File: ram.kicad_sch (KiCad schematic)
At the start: 8 parts, among them J1 ramslot1, J2 ramslot2, J3 ramslot3, J4 ramslot4, U24 74HC08, U29 74HC32, U30 74HC139

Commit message: done the pcb layout + added the 1M ram bank project
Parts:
- U24, U29: footprint Package_DIP:DIP-14_W7.62mm_Socket -> Package_DIP:DIP-14_W7.62mm
- U30: footprint (none) -> Package_DIP:DIP-16_W7.62mm
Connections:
- net BKE_{1} is gone; now on net ~{DRD}: J2.43 (Pin_43), U30.5 (O1)
- net A_{10}: now also J1.11 (Pin_11), J2.11 (Pin_11), J3.11 (Pin_11), J4.11 (Pin_11); no longer J1.12 (Pin_12), J2.12 (Pin_12), J3.12 (Pin_12), J4.12 (Pin_12)
- net A_{11}: now also J1.14 (Pin_14), J2.14 (Pin_14), J3.14 (Pin_14), J4.14 (Pin_14); no longer J1.13 (Pin_13), J2.13 (Pin_13), J3.13 (Pin_13), J4.13 (Pin_13)
- net A_{1}: now also J1.4 (Pin_4), J2.4 (Pin_4), J3.4 (Pin_4), J4.4 (Pin_4); no longer J1.3 (Pin_3), J2.3 (Pin_3), J3.3 (Pin_3), J4.3 (Pin_3)
- net A_{2}: now also J1.3 (Pin_3), J2.3 (Pin_3), J3.3 (Pin_3), J4.3 (Pin_3); no longer J1.4 (Pin_4), J2.4 (Pin_4), J3.4 (Pin_4), J4.4 (Pin_4)
- net A_{3}: now also J1.6 (Pin_6), J2.6 (Pin_6), J3.6 (Pin_6), J4.6 (Pin_6); no longer J1.5 (Pin_5), J2.5 (Pin_5), J3.5 (Pin_5), J4.5 (Pin_5)
- net A_{4}: now also J1.5 (Pin_5), J2.5 (Pin_5), J3.5 (Pin_5), J4.5 (Pin_5); no longer J1.6 (Pin_6), J2.6 (Pin_6), J3.6 (Pin_6), J4.6 (Pin_6)
- net A_{5}: now also J1.8 (Pin_8), J2.8 (Pin_8), J3.8 (Pin_8), J4.8 (Pin_8); no longer J1.7 (Pin_7), J2.7 (Pin_7), J3.7 (Pin_7), J4.7 (Pin_7)
- net A_{6}: now also J1.7 (Pin_7), J2.7 (Pin_7), J3.7 (Pin_7), J4.7 (Pin_7); no longer J1.8 (Pin_8), J2.8 (Pin_8), J3.8 (Pin_8), J4.8 (Pin_8)
- net A_{7}: now also J1.10 (Pin_10), J2.10 (Pin_10), J3.10 (Pin_10), J4.10 (Pin_10); no longer J1.9 (Pin_9), J2.9 (Pin_9), J3.9 (Pin_9), J4.9 (Pin_9)
- net A_{8}: now also J1.9 (Pin_9), J2.9 (Pin_9), J3.9 (Pin_9), J4.9 (Pin_9); no longer J1.10 (Pin_10), J2.10 (Pin_10), J3.10 (Pin_10), J4.10 (Pin_10)
- net A_{9}: now also J1.12 (Pin_12), J2.12 (Pin_12), J3.12 (Pin_12), J4.12 (Pin_12); no longer J1.11 (Pin_11), J2.11 (Pin_11), J3.11 (Pin_11), J4.11 (Pin_11)
- net DS.~{L}: now also J1.47 (Pin_47), J2.47 (Pin_47), J3.47 (Pin_47), J4.47 (Pin_47); no longer J1.48 (Pin_48), J2.48 (Pin_48), J3.48 (Pin_48), J4.48 (Pin_48)
- net DS.~{U}: now also J1.48 (Pin_48), J2.48 (Pin_48), J3.48 (Pin_48), J4.48 (Pin_48); no longer J1.47 (Pin_47), J2.47 (Pin_47), J3.47 (Pin_47), J4.47 (Pin_47)
- net D_{0}: now also J1.26 (Pin_26), J2.26 (Pin_26), J3.26 (Pin_26), J4.26 (Pin_26); no longer J1.25 (Pin_25), J2.25 (Pin_25), J3.25 (Pin_25), J4.25 (Pin_25)
- net D_{10}: now also J1.36 (Pin_36), J2.36 (Pin_36), J3.36 (Pin_36), J4.36 (Pin_36); no longer J1.35 (Pin_35), J2.35 (Pin_35), J3.35 (Pin_35), J4.35 (Pin_35)
- net D_{11}: now also J1.35 (Pin_35), J2.35 (Pin_35), J3.35 (Pin_35), J4.35 (Pin_35); no longer J1.36 (Pin_36), J2.36 (Pin_36), J3.36 (Pin_36), J4.36 (Pin_36)
- net D_{12}: now also J1.38 (Pin_38), J2.38 (Pin_38), J3.38 (Pin_38), J4.38 (Pin_38); no longer J1.37 (Pin_37), J2.37 (Pin_37), J3.37 (Pin_37), J4.37 (Pin_37)
- net D_{13}: now also J1.37 (Pin_37), J2.37 (Pin_37), J3.37 (Pin_37), J4.37 (Pin_37); no longer J1.38 (Pin_38), J2.38 (Pin_38), J3.38 (Pin_38), J4.38 (Pin_38)
- net D_{14}: now also J1.40 (Pin_40), J2.40 (Pin_40), J3.40 (Pin_40), J4.40 (Pin_40); no longer J1.39 (Pin_39), J2.39 (Pin_39), J3.39 (Pin_39), J4.39 (Pin_39)
- net D_{15}: now also J1.39 (Pin_39), J2.39 (Pin_39), J3.39 (Pin_39), J4.39 (Pin_39); no longer J1.40 (Pin_40), J2.40 (Pin_40), J3.40 (Pin_40), J4.40 (Pin_40)
- net D_{1}: now also J1.25 (Pin_25), J2.25 (Pin_25), J3.25 (Pin_25), J4.25 (Pin_25); no longer J1.26 (Pin_26), J2.26 (Pin_26), J3.26 (Pin_26), J4.26 (Pin_26)
- net D_{2}: now also J1.28 (Pin_28), J2.28 (Pin_28), J3.28 (Pin_28), J4.28 (Pin_28); no longer J1.27 (Pin_27), J2.27 (Pin_27), J3.27 (Pin_27), J4.27 (Pin_27)
- net D_{3}: now also J1.27 (Pin_27), J2.27 (Pin_27), J3.27 (Pin_27), J4.27 (Pin_27); no longer J1.28 (Pin_28), J2.28 (Pin_28), J3.28 (Pin_28), J4.28 (Pin_28)
- net D_{4}: now also J1.30 (Pin_30), J2.30 (Pin_30), J3.30 (Pin_30), J4.30 (Pin_30); no longer J1.29 (Pin_29), J2.29 (Pin_29), J3.29 (Pin_29), J4.29 (Pin_29)
- net D_{5}: now also J1.29 (Pin_29), J2.29 (Pin_29), J3.29 (Pin_29), J4.29 (Pin_29); no longer J1.30 (Pin_30), J2.30 (Pin_30), J3.30 (Pin_30), J4.30 (Pin_30)
- net D_{6}: now also J1.32 (Pin_32), J2.32 (Pin_32), J3.32 (Pin_32), J4.32 (Pin_32); no longer J1.31 (Pin_31), J2.31 (Pin_31), J3.31 (Pin_31), J4.31 (Pin_31)
- net D_{7}: now also J1.31 (Pin_31), J2.31 (Pin_31), J3.31 (Pin_31), J4.31 (Pin_31); no longer J1.32 (Pin_32), J2.32 (Pin_32), J3.32 (Pin_32), J4.32 (Pin_32)
- net D_{8}: now also J1.34 (Pin_34), J2.34 (Pin_34), J3.34 (Pin_34), J4.34 (Pin_34); no longer J1.33 (Pin_33), J2.33 (Pin_33), J3.33 (Pin_33), J4.33 (Pin_33)
- net D_{9}: now also J1.33 (Pin_33), J2.33 (Pin_33), J3.33 (Pin_33), J4.33 (Pin_33); no longer J1.34 (Pin_34), J2.34 (Pin_34), J3.34 (Pin_34), J4.34 (Pin_34)
- net E_{0}: now also J1.21 (Pin_21), J2.21 (Pin_21), J3.21 (Pin_21), J4.21 (Pin_21); no longer J1.22 (Pin_22), J2.22 (Pin_22), J3.22 (Pin_22), J4.22 (Pin_22)
- net E_{10}: now also J1.15 (Pin_15), J2.15 (Pin_15), J3.15 (Pin_15), J4.15 (Pin_15); no longer J1.16 (Pin_16), J2.16 (Pin_16), J3.16 (Pin_16), J4.16 (Pin_16)
- net E_{11}: now also J1.18 (Pin_18), J2.18 (Pin_18), J3.18 (Pin_18), J4.18 (Pin_18); no longer J1.17 (Pin_17), J2.17 (Pin_17), J3.17 (Pin_17), J4.17 (Pin_17)
- net E_{12}: now also J1.17 (Pin_17), J2.17 (Pin_17), J3.17 (Pin_17), J4.17 (Pin_17); no longer J1.18 (Pin_18), J2.18 (Pin_18), J3.18 (Pin_18), J4.18 (Pin_18)
- net E_{13}: now also J1.20 (Pin_20), J2.20 (Pin_20), J3.20 (Pin_20), J4.20 (Pin_20); no longer J1.19 (Pin_19), J2.19 (Pin_19), J3.19 (Pin_19), J4.19 (Pin_19)
- net E_{14}: now also J1.19 (Pin_19), J2.19 (Pin_19), J3.19 (Pin_19), J4.19 (Pin_19); no longer J1.20 (Pin_20), J2.20 (Pin_20), J3.20 (Pin_20), J4.20 (Pin_20)
- net E_{15}: now also J1.22 (Pin_22), J2.22 (Pin_22), J3.22 (Pin_22), J4.22 (Pin_22); no longer J1.21 (Pin_21), J2.21 (Pin_21), J3.21 (Pin_21), J4.21 (Pin_21)
- net E_{1}: now also J1.24 (Pin_24), J2.24 (Pin_24), J3.24 (Pin_24), J4.24 (Pin_24); no longer J1.23 (Pin_23), J2.23 (Pin_23), J3.23 (Pin_23), J4.23 (Pin_23)
- net E_{8}: now also J1.13 (Pin_13), J2.13 (Pin_13), J3.13 (Pin_13), J4.13 (Pin_13); no longer J1.14 (Pin_14), J2.14 (Pin_14), J3.14 (Pin_14), J4.14 (Pin_14)
- net E_{9}: now also J1.16 (Pin_16), J2.16 (Pin_16), J3.16 (Pin_16), J4.16 (Pin_16); no longer J1.15 (Pin_15), J2.15 (Pin_15), J3.15 (Pin_15), J4.15 (Pin_15)
- net GND: now also J1.23 (Pin_23), J2.23 (Pin_23), J3.23 (Pin_23), J4.23 (Pin_23); no longer J1.24 (Pin_24), J2.24 (Pin_24), J3.24 (Pin_24), J4.24 (Pin_24)
- net PDIR.~{R}: now also J1.45 (Pin_45), J2.45 (Pin_45), J3.45 (Pin_45), J4.45 (Pin_45); no longer J1.46 (Pin_46), J2.46 (Pin_46), J3.46 (Pin_46), J4.46 (Pin_46)
- net PDIR.~{W}: now also J1.46 (Pin_46), J2.46 (Pin_46), J3.46 (Pin_46), J4.46 (Pin_46); no longer J1.45 (Pin_45), J2.45 (Pin_45), J3.45 (Pin_45), J4.45 (Pin_45)
- net ~{DRD}: now also J1.43 (Pin_43), J3.43 (Pin_43), J4.43 (Pin_43); no longer J1.44 (Pin_44), J3.44 (Pin_44), J4.44 (Pin_44)
- net BKE_{0} renamed ~{BKE_{0}}
- net ~{BKE_{0}}: now also J1.44 (Pin_44); no longer J1.43 (Pin_43)
- net BKE_{2} renamed ~{BKE_{2}}
- net ~{BKE_{2}}: now also J3.44 (Pin_44); no longer J3.43 (Pin_43)
- net BKE_{3} renamed ~{BKE_{3}}
- net ~{BKE_{3}}: now also J4.44 (Pin_44); no longer J4.43 (Pin_43)

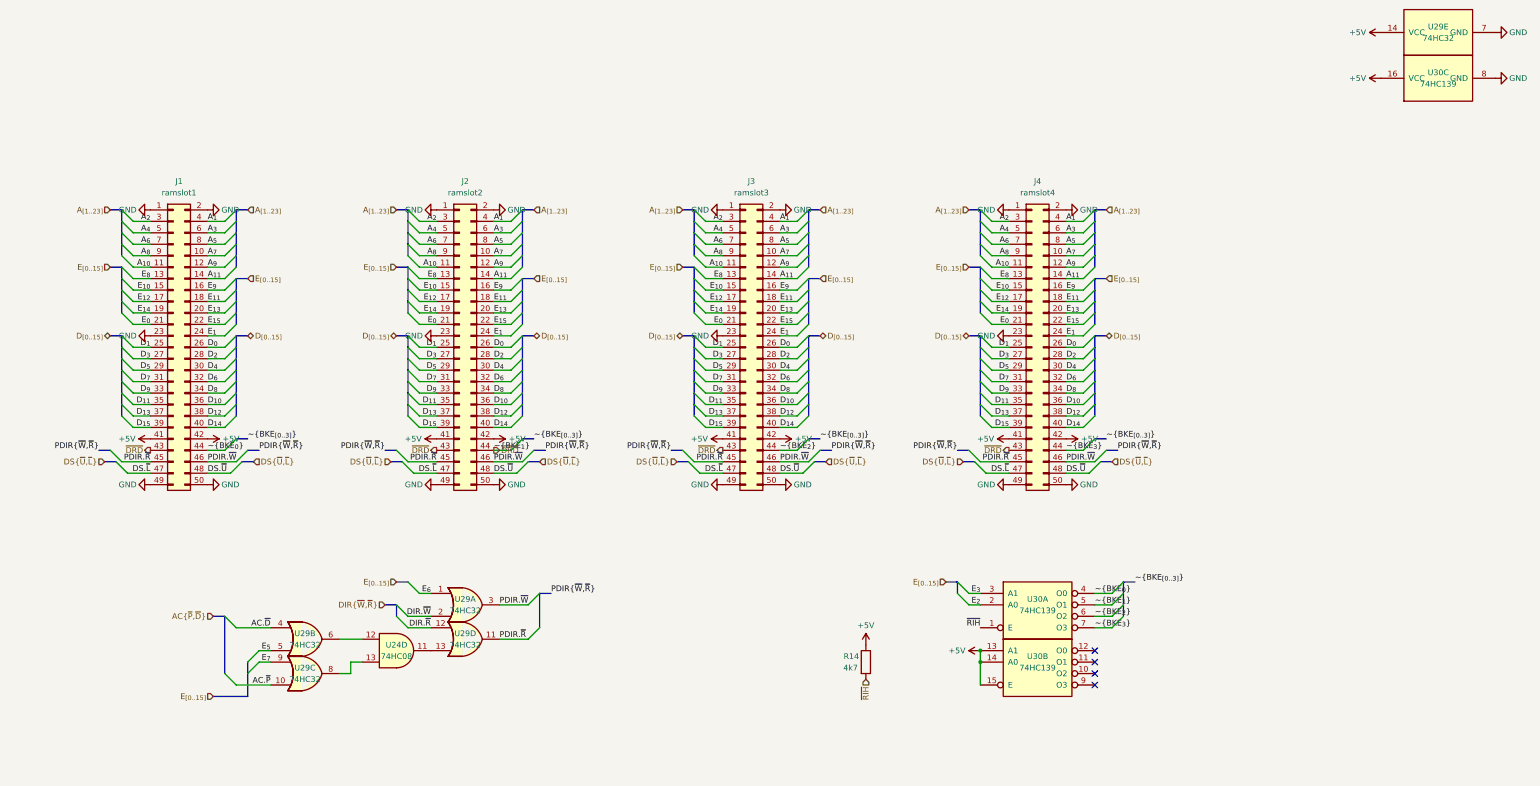
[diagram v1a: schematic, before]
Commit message: updated scheme: 	- fixed E to P & PRT mapping 	- swapped root's 04 couple with the 14's of pidreg & statusreg
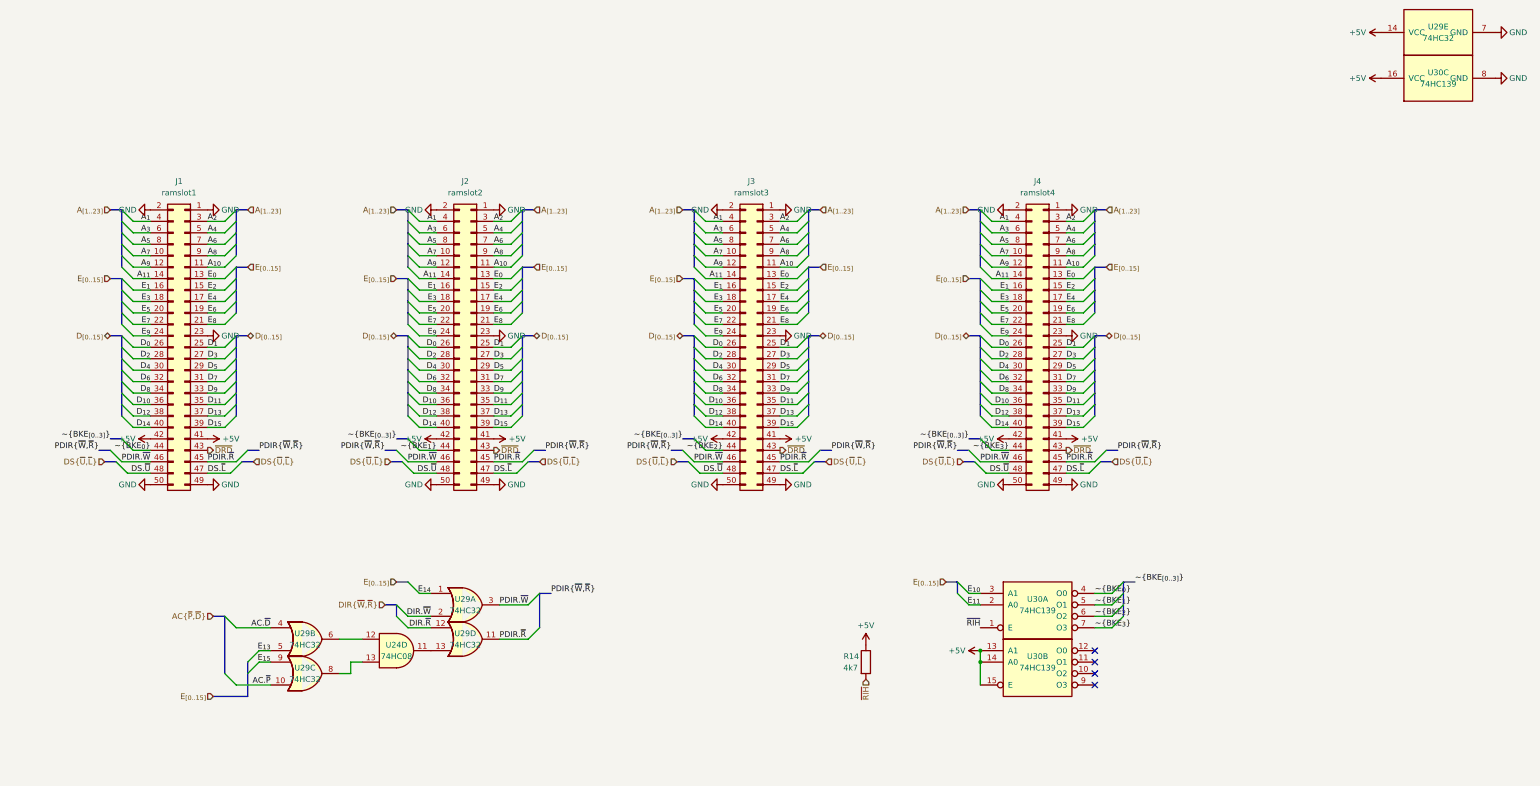
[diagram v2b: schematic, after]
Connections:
- net E_{0}: now also J1.13 (Pin_13), J2.13 (Pin_13), J3.13 (Pin_13), J4.13 (Pin_13); no longer J1.21 (Pin_21), J2.21 (Pin_21), J3.21 (Pin_21), J4.21 (Pin_21)
- net E_{10}: now also U30.3 (A1); no longer J1.15 (Pin_15), J2.15 (Pin_15), J3.15 (Pin_15), J4.15 (Pin_15)
- net E_{11}: now also U30.2 (A0); no longer J1.18 (Pin_18), J2.18 (Pin_18), J3.18 (Pin_18), J4.18 (Pin_18)
- net E_{13}: now also U29.5; no longer J1.20 (Pin_20), J2.20 (Pin_20), J3.20 (Pin_20), J4.20 (Pin_20)
- net E_{14}: now also U29.1; no longer J1.19 (Pin_19), J2.19 (Pin_19), J3.19 (Pin_19), J4.19 (Pin_19)
- net E_{15}: now also U29.9; no longer J1.22 (Pin_22), J2.22 (Pin_22), J3.22 (Pin_22), J4.22 (Pin_22)
- net E_{1}: now also J1.16 (Pin_16), J2.16 (Pin_16), J3.16 (Pin_16), J4.16 (Pin_16); no longer J1.24 (Pin_24), J2.24 (Pin_24), J3.24 (Pin_24), J4.24 (Pin_24)
- net E_{2}: now also J1.15 (Pin_15), J2.15 (Pin_15), J3.15 (Pin_15), J4.15 (Pin_15); no longer U30.2 (A0)
- net E_{3}: now also J1.18 (Pin_18), J2.18 (Pin_18), J3.18 (Pin_18), J4.18 (Pin_18); no longer U30.3 (A1)
- net E_{5}: now also J1.20 (Pin_20), J2.20 (Pin_20), J3.20 (Pin_20), J4.20 (Pin_20); no longer U29.5
- net E_{6}: now also J1.19 (Pin_19), J2.19 (Pin_19), J3.19 (Pin_19), J4.19 (Pin_19); no longer U29.1
- net E_{7}: now also J1.22 (Pin_22), J2.22 (Pin_22), J3.22 (Pin_22), J4.22 (Pin_22); no longer U29.9
- net E_{8}: now also J1.21 (Pin_21), J2.21 (Pin_21), J3.21 (Pin_21), J4.21 (Pin_21); no longer J1.13 (Pin_13), J2.13 (Pin_13), J3.13 (Pin_13), J4.13 (Pin_13)
- net E_{9}: now also J1.24 (Pin_24), J2.24 (Pin_24), J3.24 (Pin_24), J4.24 (Pin_24); no longer J1.16 (Pin_16), J2.16 (Pin_16), J3.16 (Pin_16), J4.16 (Pin_16)
- net ~{DRD}: no longer J2.44 (Pin_44), U30.5 (O1)
- net E_{12} renamed E_{4}
- new net ~{BKE_{1}}: J2.44 (Pin_44), U30.5 (O1)

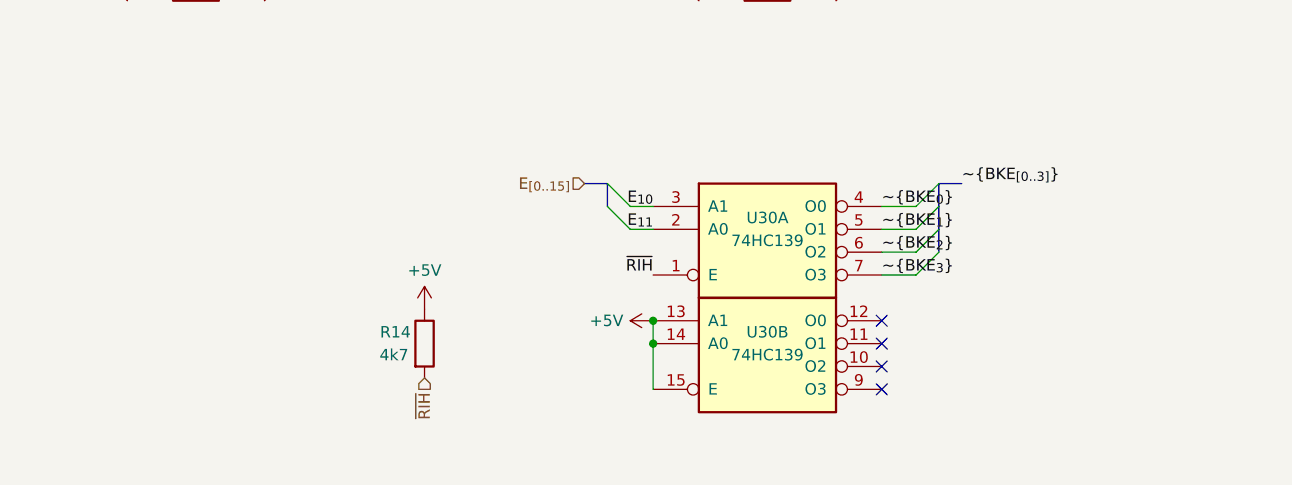
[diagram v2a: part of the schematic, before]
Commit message: apparently the ram was enabled all the time, ram.kicad_sch didn't even require BE.M... 	like whaaaaaaaa how did i let this happen oh my god sometimes im just braindead.
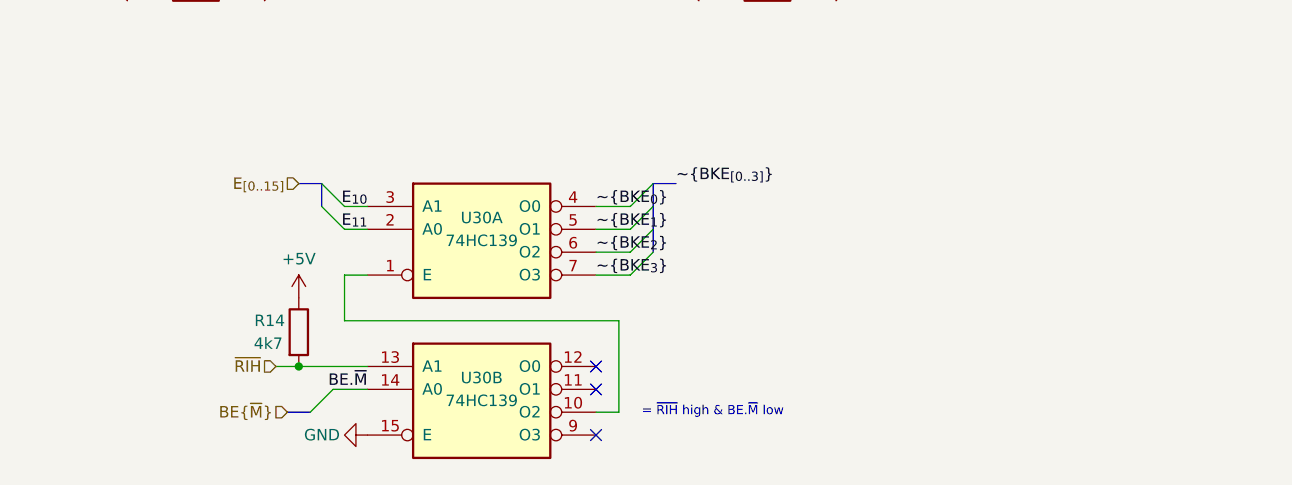
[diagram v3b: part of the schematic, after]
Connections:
- net +5V: no longer U30.13 (A1), U30.14 (A0), U30.15 (E)
- net GND: now also U30.15 (E)
- net ~{RIH}: now also U30.13 (A1); no longer U30.1 (E)
- net at U30.10 (O2): now also U30.1 (E)
- new net BE.~{M}: U30.14 (A0)
- no-connect marks 4 -> 3
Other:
- note added: "= ~{RIH} high & BE.~{M} low"
- moved on the sheet: R14, U30A, U30B
